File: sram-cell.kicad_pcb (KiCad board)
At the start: 2 copper layers, 50.8 x 50.8 mm, 64 parts, among them J1 USB_B_Micro, J2 PowerHeader, Q1 PMOS_GSD, Q10 NMOS_GSD, Q11 NMOS_GSD, Q2 PMOS_GSD, Q3 NMOS_GSD, Q4 NMOS_GSD, Q5 NMOS_GSD, Q6 NMOS_GSD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

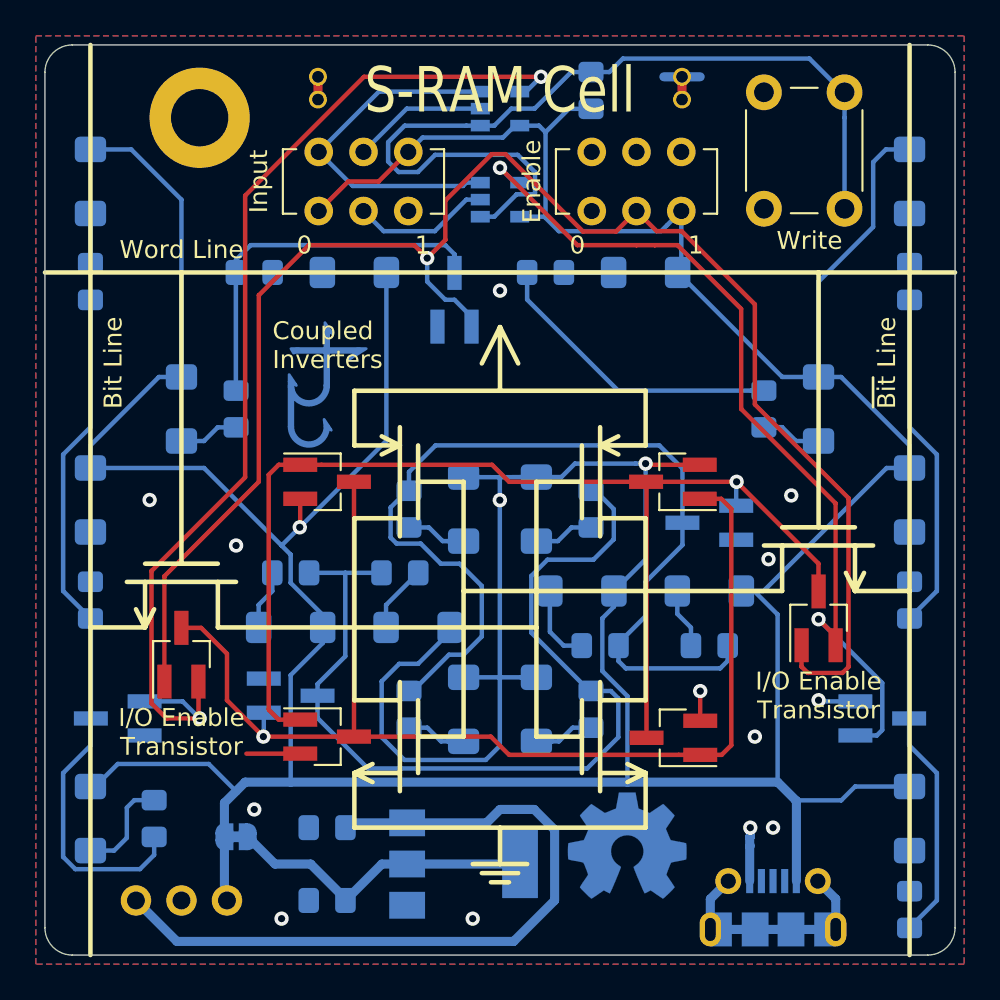
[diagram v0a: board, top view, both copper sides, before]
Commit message: don't use radius zero circles on the silkscreen
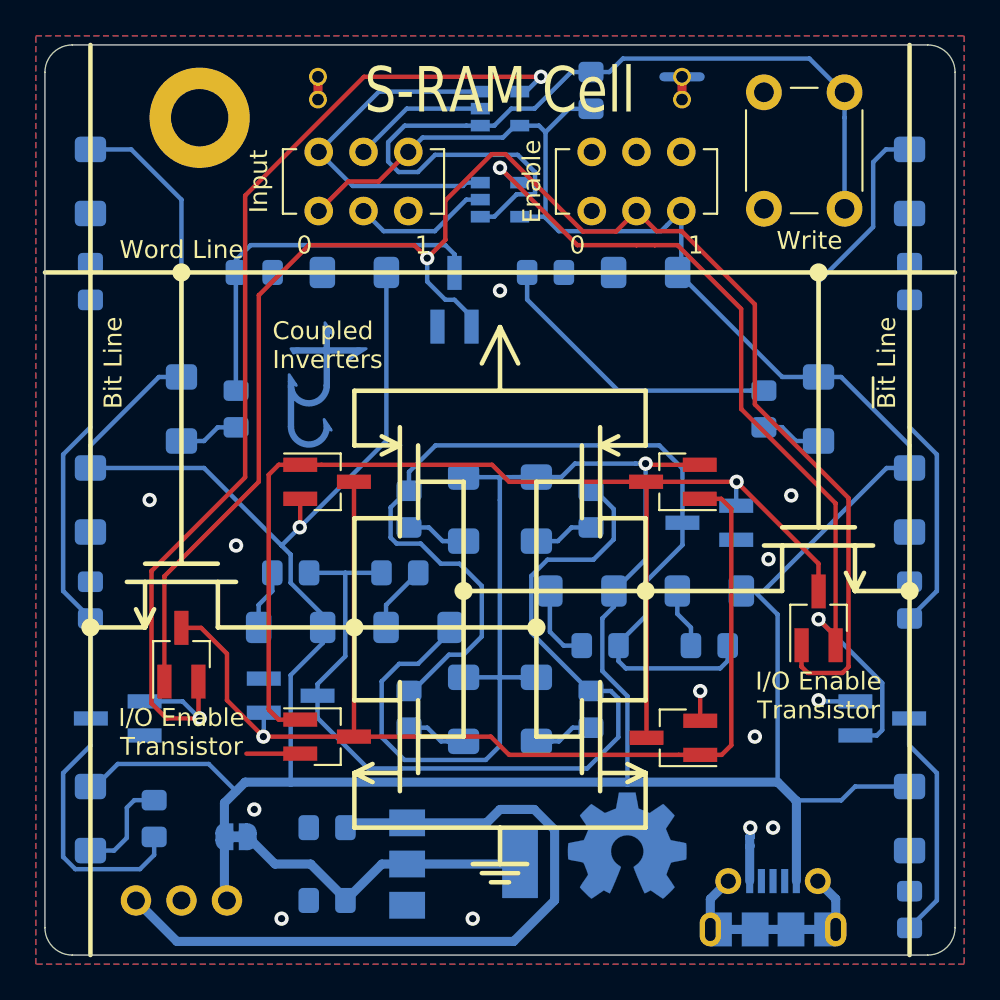
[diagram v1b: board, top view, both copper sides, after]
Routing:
- net VCC: vias 3 -> 2
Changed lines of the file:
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@@
     (thickness 1.6)
     (drawings 101)
-    (tracks 441)
+    (tracks 440)
     (zones 0)
     (modules 64)
@@
     (pcbplotparams
       (layerselection 0x010f0_ffffffff)
-      (usegerberextensions false)
+      (usegerberextensions true)
       (usegerberattributes false)
       (usegerberadvancedattributes false)
@@
     )
   )
+  (gr_circle (center 170.18 88.9) (end 170.434 88.9) (layer F.SilkS) (width 0.508))
+  (gr_circle (center 134.62 88.9) (end 134.874 88.9) (layer F.SilkS) (width 0.508))
+  (gr_circle (center 129.54 108.712) (end 129.794 108.712) (layer F.SilkS) (width 0.508))
+  (gr_circle (center 175.26 106.68) (end 175.514 106.68) (layer F.SilkS) (width 0.508))
+  (gr_circle (center 144.272 108.712) (end 144.526 108.712) (layer F.SilkS) (width 0.508))
+  (gr_circle (center 160.528 106.68) (end 160.782 106.68) (layer F.SilkS) (width 0.508))
+  (gr_circle (center 154.432 108.712) (end 154.686 108.712) (layer F.SilkS) (width 0.508))
+  (gr_circle (center 150.368 106.68) (end 150.622 106.68) (layer F.SilkS) (width 0.508))
   (gr_text "github.com/tyehle/sram-cell\n" (at 155.321 126.111) (layer B.SilkS)
     (effects (font (size 0.762 0.5842) (thickness 0.127)) (justify left mirror))
@@
   )
   (gr_arc (start 128.524 77.724) (end 128.524 76.2) (angle -90) (layer Edge.Cuts) (width 0.0254))
-  (gr_circle (center 170.18 88.9) (end 170.18 88.9) (layer F.SilkS) (width 1.016))
-  (gr_circle (center 134.62 88.9) (end 134.62 88.9) (layer F.SilkS) (width 1.016))
   (gr_line (start 127 88.9) (end 177.8 88.9) (layer F.SilkS) (width 0.254))
   (gr_line (start 175.26 127) (end 175.26 76.2) (layer F.SilkS) (width 0.254))
   (gr_line (start 129.54 127) (end 129.54 76.2) (layer F.SilkS) (width 0.254))
-  (gr_circle (center 129.54 108.712) (end 129.54 108.712) (layer F.SilkS) (width 1.016))
-  (gr_circle (center 175.26 106.68) (end 175.26 106.68) (layer F.SilkS) (width 1.016))
   (gr_line (start 173.228 104.14) (end 167.132 104.14) (layer F.SilkS) (width 0.254))
   (gr_line (start 172.212 103.124) (end 168.148 103.124) (layer F.SilkS) (width 0.254))
@@
   (gr_line (start 144.272 95.504) (end 160.528 95.504) (layer F.SilkS) (width 0.254))
   (gr_line (start 160.528 119.888) (end 144.272 119.888) (layer F.SilkS) (width 0.254))
-  (gr_circle (center 144.272 108.712) (end 144.272 108.712) (layer F.SilkS) (width 1.016))
-  (gr_circle (center 154.432 108.712) (end 154.432 108.712) (layer F.SilkS) (width 1.016))
-  (gr_circle (center 150.368 106.68) (end 150.368 106.68) (layer F.SilkS) (width 1.016))
-  (gr_circle (center 160.528 106.68) (end 160.528 106.68) (layer F.SilkS) (width 1.016))
   (gr_line (start 144.272 108.712) (end 154.432 108.712) (layer F.SilkS) (width 0.254))
   (gr_line (start 160.528 106.68) (end 150.368 106.68) (layer F.SilkS) (width 0.254))
@@
   (segment (start 152.3905 111.4965) (end 150.368 111.4965) (width 0.25) (layer B.Cu) (net 3))
   (segment (start 152.3905 101.6095) (end 152.3905 100.3395) (width 0.25) (layer B.Cu) (net 3))
-  (via (at 152.3905 101.6095) (size 0.8) (drill 0.4) (layers F.Cu B.Cu) (net 3))
   (segment (start 134.62 94.02) (end 134.62 94.7325) (width 0.25) (layer B.Cu) (net 3))
   (segment (start 134.62 84.836) (end 134.62 94.02) (width 0.25) (layer B.Cu) (net 3))
